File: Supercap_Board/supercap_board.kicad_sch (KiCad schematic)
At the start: 4 parts

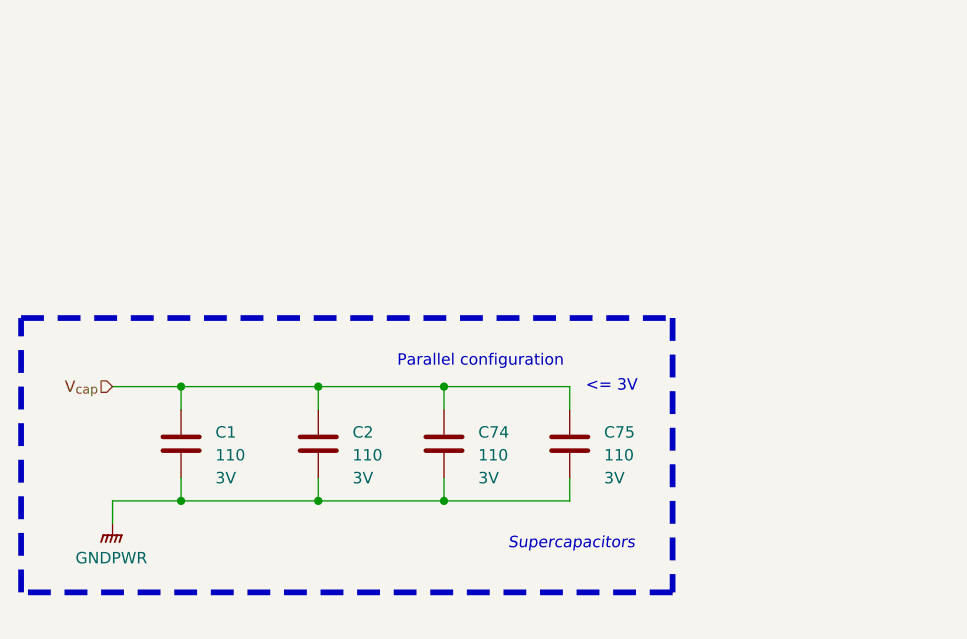
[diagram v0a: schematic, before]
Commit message: switched capacitor topology to 4S
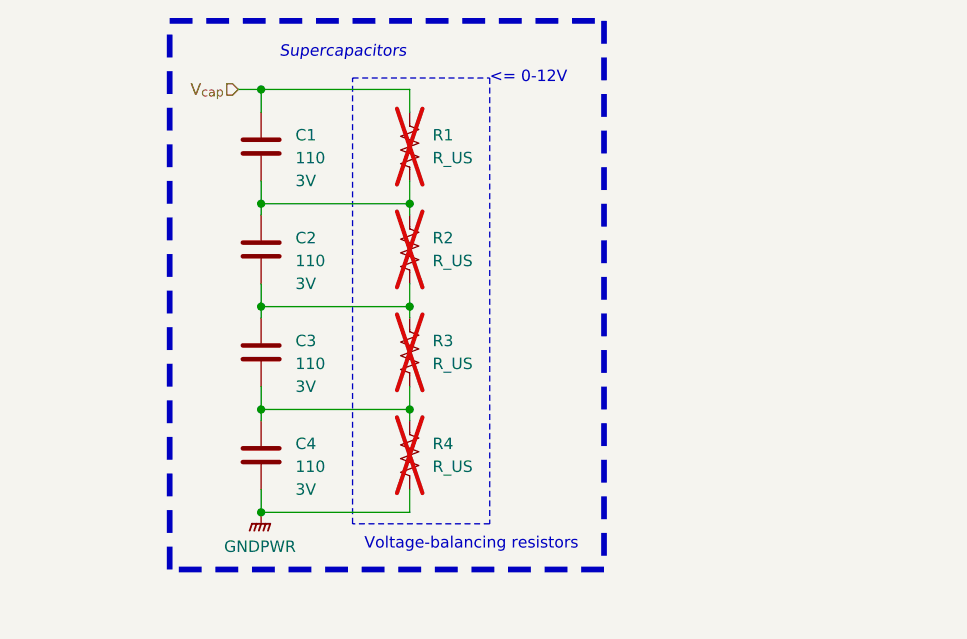
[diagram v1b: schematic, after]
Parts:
- added R1, R2, R3, R4: R_US, symbol Device:R_US
- renumbered C74 to C3, C75 to C4
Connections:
- net GNDPWR: now also R4.2; no longer C1.2, C2.2, C3.2
- net V_{cap}: now also R1.1; no longer C2.1, C3.1, C4.1
- new net: C1.2, C2.1, R1.2, R2.1
- new net: C2.2, C3.1, R2.2, R3.1
- new net: C3.2, C4.1, R3.2, R4.1
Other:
- note added: "<= 0-12V"
- note added: "Voltage-balancing resistors"
- note removed: "<= 3V"
- note removed: "Parallel configuration"
- moved on the sheet: C1, C2, C3, C4

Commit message: changed converter topology to full-bridge design
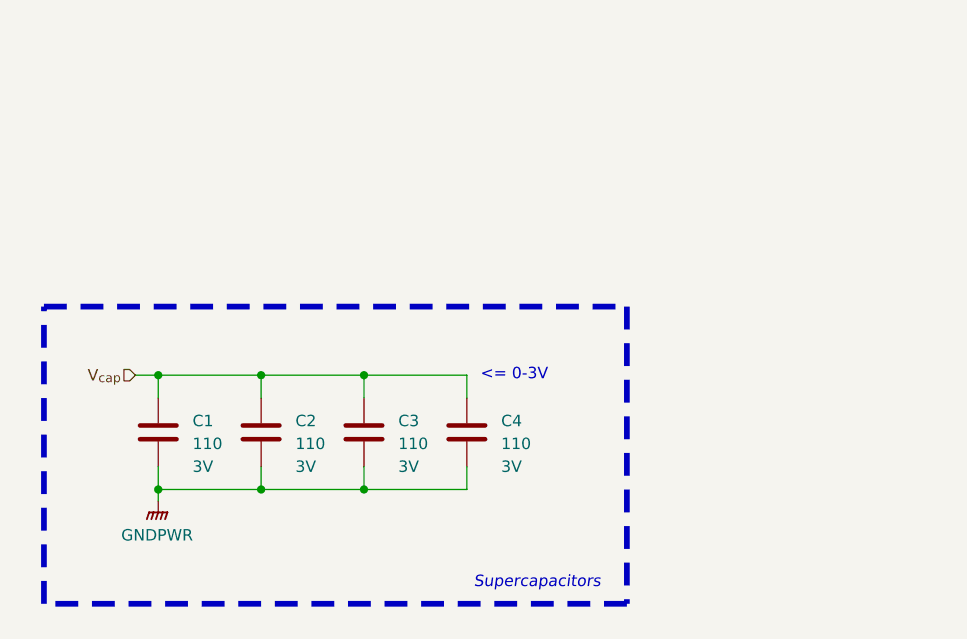
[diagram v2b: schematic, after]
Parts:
- removed R1, R2, R3, R4: R_US, symbol Device:R_US
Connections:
- net GNDPWR: now also C1.2, C2.2, C3.2
- net V_{cap}: now also C2.1, C3.1, C4.1
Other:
- note added: "<= 0-3V"
- note removed: "<= 0-12V"
- note removed: "Voltage-balancing resistors"
- moved on the sheet: C1, C2, C3, C4

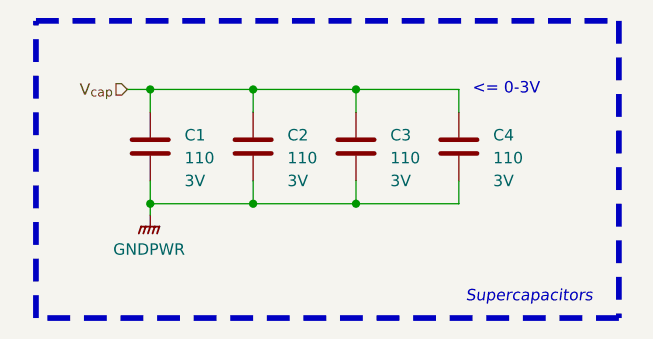
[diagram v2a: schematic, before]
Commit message: fixed converter section
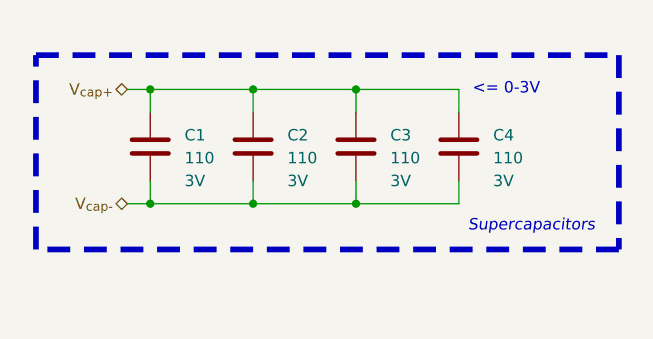
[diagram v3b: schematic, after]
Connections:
- net GNDPWR renamed V_{cap-}
- net V_{cap} renamed V_{cap+}
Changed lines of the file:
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@@
 	)
 	(rectangle
-		(start 73.66 48.26)
-		(end 138.43 81.28)
+		(start 73.66 52.07)
+		(end 138.43 73.66)
 		(stroke
 			(width 0.635)
@@
 	(text "Supercapacitors"
 		(exclude_from_sim no)
-		(at 121.412 78.232 0)
+		(at 121.666 70.358 0)
 		(effects
 			(font
@@
 	)
 	(junction
+		(at 97.79 55.88)
+		(diameter 0)
+		(color 0 0 0 0)
+	)
+	(junction
 		(at 86.36 68.58)
 		(diameter 0)
@@
 	)
 	(junction
-		(at 97.79 55.88)
-		(diameter 0)
-		(color 0 0 0 0)
-	)
-	(junction
 		(at 97.79 68.58)
 		(diameter 0)
@@
 	(wire
 		(pts
+			(xy 83.82 68.58) (xy 86.36 68.58)
+		)
+		(stroke
+			(width 0)
+			(type default)
+		)
+	)
+	(wire
+		(pts
 			(xy 109.22 58.42) (xy 109.22 55.88)
 		)
@@
 	(wire
 		(pts
-			(xy 86.36 68.58) (xy 86.36 69.85)
-		)
-		(stroke
-			(width 0)
-			(type default)
-		)
-	)
-	(wire
-		(pts
 			(xy 109.22 68.58) (xy 120.65 68.58)
 		)
@@
 		)
 	)
-	(hierarchical_label "V_{cap}"
-		(shape input)
+	(hierarchical_label "V_{cap+}"
+		(shape bidirectional)
 		(at 83.82 55.88 180)
+		(effects
+			(font
+				(size 1.27 1.27)
+			)
+			(justify right)
+		)
+	)
+	(hierarchical_label "V_{cap-}"
+		(shape bidirectional)
+		(at 83.82 68.58 180)
 		(effects
 			(font
@@
 					(unit 1)
 				)
-			)
-		)
-	)
-	(symbol
-		(lib_id "power:GNDPWR")
-		(at 86.36 69.85 0)
-		(unit 1)
-		(exclude_from_sim no)
-		(in_bom yes)
-		(on_board yes)
-		(dnp no)
-		(fields_autoplaced yes)
-		(property "Reference" "#PWR05"
-			(at 86.36 74.93 0)
-			(effects
-				(font
-					(size 1.27 1.27)
-				)
-				(hide yes)
-			)
-		)
-		(property "Value" "GNDPWR"
-			(at 86.233 73.66 0)
-			(effects
-				(font
-					(size 1.27 1.27)
-				)
-			)
-		)
-		(property "Footprint" ""
-			(at 86.36 71.12 0)
-			(effects
-				(font
-					(size 1.27 1.27)
-				)
-				(hide yes)
-			)
-		)
-		(property "Datasheet" ""
-			(at 86.36 71.12 0)
-			(effects
-				(font
-					(size 1.27 1.27)
-				)
-				(hide yes)
-			)
-		)
-		(property "Description" "Power symbol creates a global label with name \"GNDPWR\" , global ground"
-			(at 86.36 69.85 0)
-			(effects
-				(font
-					(size 1.27 1.27)
-				)
-				(hide yes)
-			)
-		)
-		(pin "1"
-		)
-		(instances
-			(project ""
-				(path "/98ee8313-37ab-4329-91ab-b5710476f82f/79ba0ad0-1263-4d7e-82bc-d7cd5a71cdbf"
-					(reference "#PWR05")
-					(unit 1)
-				)

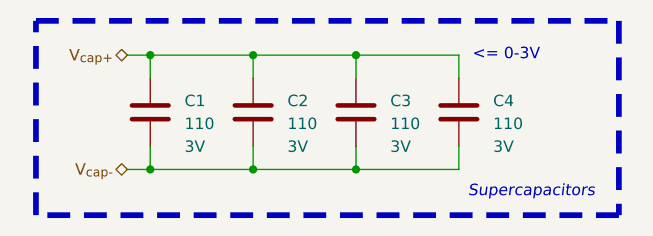
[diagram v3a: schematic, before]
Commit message: removed v1 files and assigned mouser part numbers
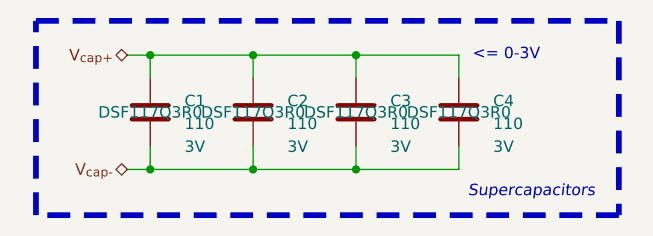
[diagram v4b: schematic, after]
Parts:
- C1, C2, C3, C4: Manufacturer_Part_Number (none) -> DSF117Q3R0; now left out of the parts list
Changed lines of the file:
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@@
 		(unit 1)
 		(exclude_from_sim no)
-		(in_bom yes)
+		(in_bom no)
 		(on_board yes)
 		(dnp no)
@@
 				)
 				(justify left)
+			)
+		)
+		(property "Manufacturer_Part_Number" "DSF117Q3R0"
+			(at 97.79 62.23 0)
+			(effects
+				(font
+					(size 1.27 1.27)
+				)
 			)
 		)
@@
 		(unit 1)
 		(exclude_from_sim no)
-		(in_bom yes)
+		(in_bom no)
 		(on_board yes)
 		(dnp no)
@@
 				)
 				(justify left)
+			)
+		)
+		(property "Manufacturer_Part_Number" "DSF117Q3R0"
+			(at 86.36 62.23 0)
+			(effects
+				(font
+					(size 1.27 1.27)
+				)
 			)
 		)
@@
 		(unit 1)
 		(exclude_from_sim no)
-		(in_bom yes)
+		(in_bom no)
 		(on_board yes)
 		(dnp no)
@@
 				)
 				(justify left)
+			)
+		)
+		(property "Manufacturer_Part_Number" "DSF117Q3R0"
+			(at 109.22 62.23 0)
+			(effects
+				(font
+					(size 1.27 1.27)
+				)
 			)
 		)
@@
 		(unit 1)
 		(exclude_from_sim no)
-		(in_bom yes)
+		(in_bom no)
 		(on_board yes)
 		(dnp no)
@@
 			)
 		)
+		(property "Manufacturer_Part_Number" "DSF117Q3R0"
+			(at 120.65 62.23 0)
+			(effects
+				(font
+					(size 1.27 1.27)
+				)
+			)
+		)

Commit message: began layout
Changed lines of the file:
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@@
 				)
 				(justify left)
+				(hide yes)
 			)
 		)
@@
 					(size 1.27 1.27)
 				)
+				(hide yes)
 			)
 		)
@@
 				)
 				(justify left)
+				(hide yes)
 			)
 		)
@@
 					(size 1.27 1.27)
 				)
+				(hide yes)
 			)
 		)
@@
 				)
 				(justify left)
+				(hide yes)
 			)
 		)
@@
 					(size 1.27 1.27)
 				)
+				(hide yes)
 			)
 		)
@@
 				)
 				(justify left)
+				(hide yes)
 			)
 		)
@@
 					(size 1.27 1.27)
 				)
-			)
-		)
+				(hide yes)
+			)
+		)

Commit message: mostly done with first order layout
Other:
- title: Supercapacitor + Balancing -> Supercapacitor Board
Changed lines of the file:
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@@
 	(paper "A5")
 	(title_block
-		(title "Supercapacitor + Balancing")
+		(title "Supercapacitor Board")
 		(date "2025-02-12")
-		(rev "1")
+		(rev "2")
 		(company "UT Robomaster")
 		(comment 1 "Robomaster")
@@
 			)
 		)
-		(property "Datasheet" "https://www.mouser.com/datasheet/2/40/AVX_SCC-3084824.pdf"
+		(property "Datasheet" "https://www.cde.com/resources/catalogs/DSF.pdf"
 			(at 97.79 62.23 0)
 			(effects
@@
 			)
 		)
-		(property "Datasheet" "https://www.mouser.com/datasheet/2/40/AVX_SCC-3084824.pdf"
+		(property "Datasheet" "https://www.cde.com/resources/catalogs/DSF.pdf"
 			(at 86.36 62.23 0)
 			(effects
@@
 			)
 		)
-		(property "Datasheet" "https://www.mouser.com/datasheet/2/40/AVX_SCC-3084824.pdf"
+		(property "Datasheet" "https://www.cde.com/resources/catalogs/DSF.pdf"
 			(at 109.22 62.23 0)
 			(effects
@@
 			)
 		)
-		(property "Datasheet" "https://www.mouser.com/datasheet/2/40/AVX_SCC-3084824.pdf"
+		(property "Datasheet" "https://www.cde.com/resources/catalogs/DSF.pdf"
 			(at 120.65 62.23 0)
 			(effects

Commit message: big progress on layout
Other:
- note added: "Notes: - Capacitors are mounted sideways relative to board, so upright relative to gravity - Bodies of capacitors are secured to board via adhesive/brackets - 1980J of energy storage => ideal charging time of 22 seconds under no load"
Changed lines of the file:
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@@
+		)
+	)
+	(text "Notes:\n- Capacitors are mounted sideways relative to board, so upright relative to gravity\n- Bodies of capacitors are secured to board via adhesive/brackets\n- 1980J of energy storage => ideal charging time of 22 seconds under no load"
+		(exclude_from_sim no)
+		(at 73.787 78.994 0)
+		(effects
+			(font
+				(size 1.27 1.27)
+			)
+			(justify left)
+		)
+	)
+	(text "Supercapacitors"
+		(exclude_from_sim no)
+		(at 137.16 71.628 0)
+		(effects
+			(font
+				(size 1.905 1.905)
+			)
+			(justify right)
 		)
 	)
@@
 		)
 	)
-	(text "Supercapacitors"
-		(exclude_from_sim no)
-		(at 121.666 70.358 0)
-		(effects
-			(font
-				(size 1.27 1.27)
-				(italic yes)
-			)
-			(justify left top)
-		)
-	)
